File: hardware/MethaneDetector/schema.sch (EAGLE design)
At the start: 19 parts, among them IC1 AT90S2313P, Q1 2N4401, Q2 2N4401

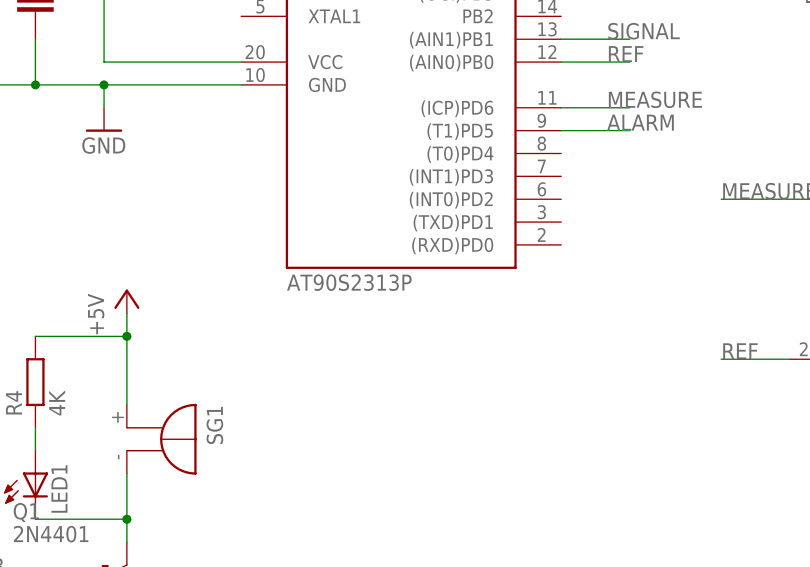
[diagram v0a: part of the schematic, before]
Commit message: small component name fix
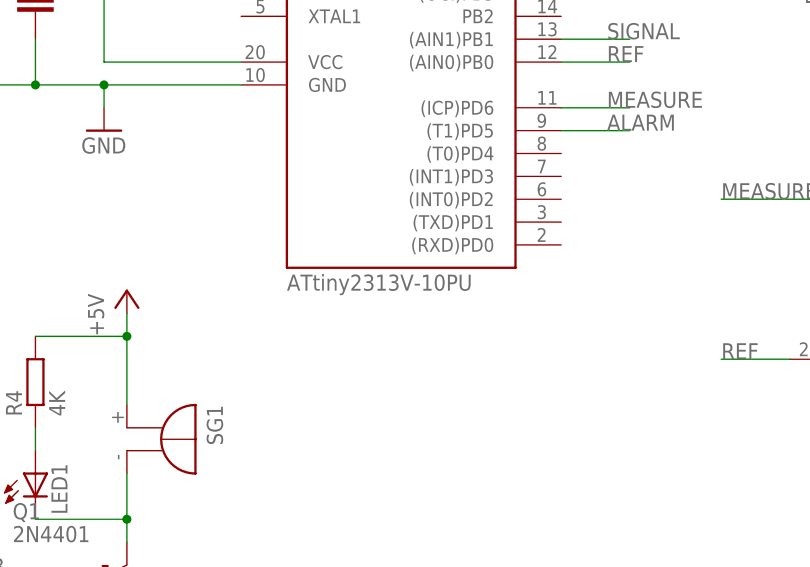
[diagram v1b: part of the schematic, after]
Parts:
- IC1: value AT90S2313P -> ATtiny2313V-10PU
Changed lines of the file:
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@@
 </classes>
 <parts>
-<part name="IC1" library="atmel" deviceset="AT90S2313" device="P"/>
+<part name="IC1" library="atmel" deviceset="AT90S2313" device="P" value="ATtiny2313V-10PU"/>
 <part name="SEN1" library="SparkFun-Sensors" deviceset="METHANE_SENSOR" device=""/>
 <part name="SG1" library="buzzer" deviceset="BMT1205XH7.5" device="" value=""/>
